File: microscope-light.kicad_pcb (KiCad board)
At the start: 2 copper layers, 72 x 100 mm, 57 parts, among them J1 USB_C_Receptacle_USB2.0, J2 TagConnect_TC2030_SWD, SW1 WARM, SW2 COLD, SW3 BRIGHT, SW4 DIM, U1 SY7200A, U2 SY7200A, U3 STM32F030F4Px, U4 XC6206PxxxMR

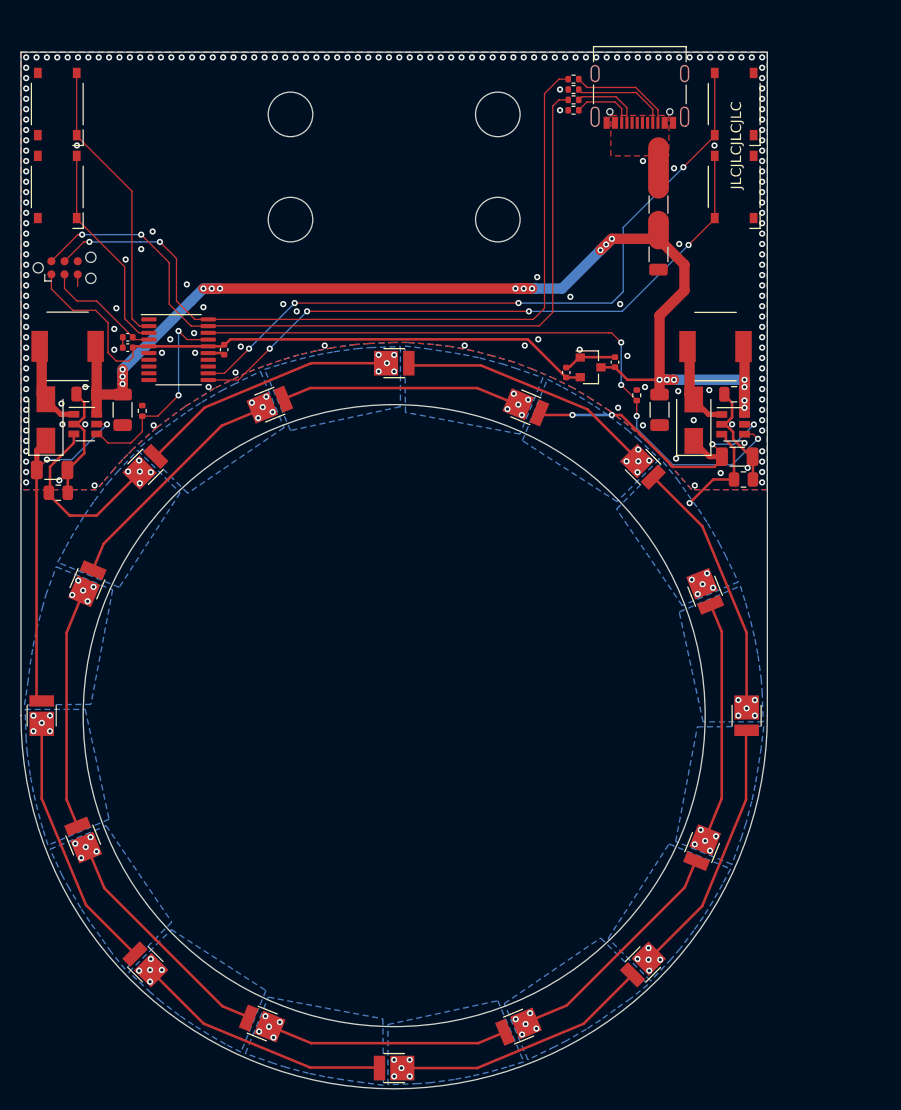
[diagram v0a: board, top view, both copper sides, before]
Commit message: Add fabrication features
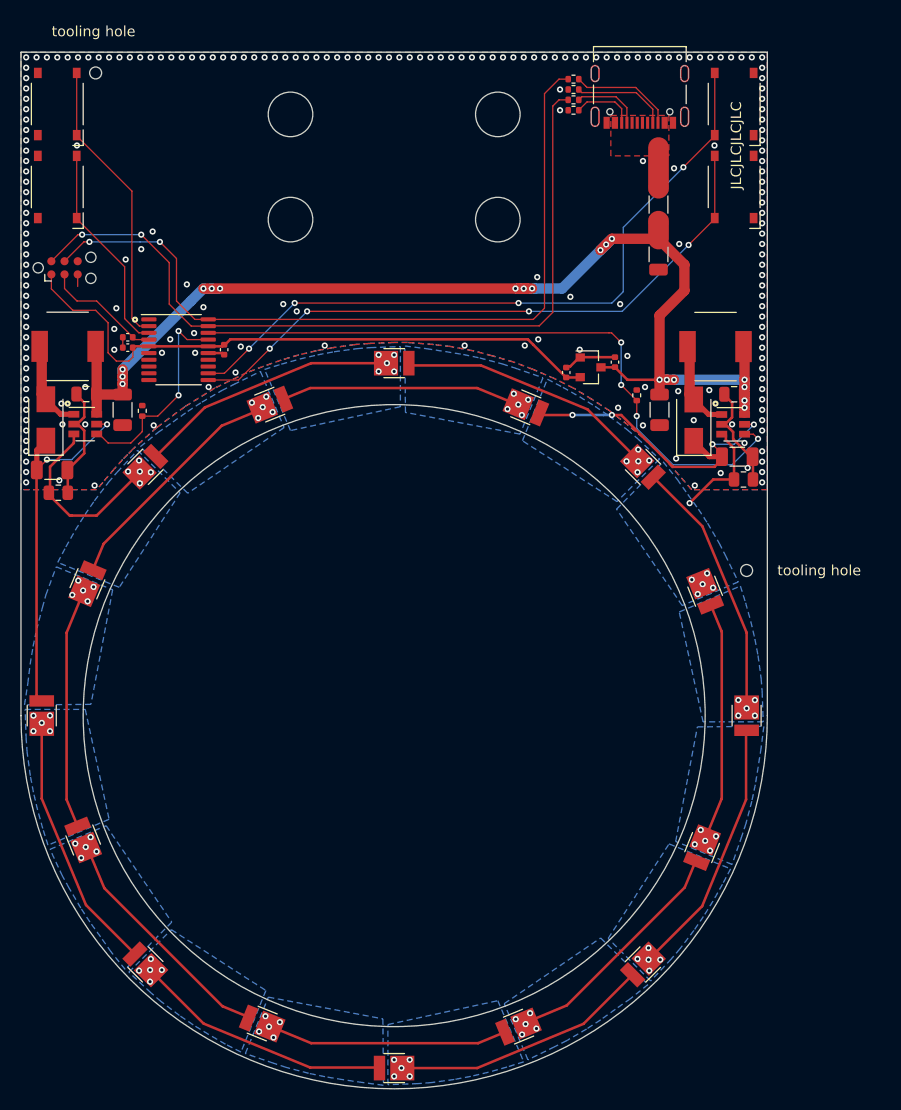
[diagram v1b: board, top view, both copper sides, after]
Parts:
- added H5: ToolingHole, ToolingHole:ToolingHole_JLCSMT, F.Cu at (164.0, 100.0)
- added H6: ToolingHole, ToolingHole:ToolingHole_JLCSMT, F.Cu at (101.2, 52.0)
- D10, D12, D14, D16, D2, D4, D6, D8: value LED -> LEDC
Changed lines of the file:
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@@
   (general
     (thickness 1.6)
-    (drawings 19)
+    (drawings 22)
     (tracks 626)
     (zones 0)
-    (modules 57)
+    (modules 59)
     (nets 50)
   )
@@
     (pcbplotparams
       (layerselection 0x010fc_ffffffff)
-      (usegerberextensions false)
+      (usegerberextensions true)
       (usegerberattributes true)
       (usegerberadvancedattributes true)
-      (creategerberjobfile true)
+      (creategerberjobfile false)
       (excludeedgelayer true)
       (linewidth 0.100000)
@@
       (outputformat 1)
       (mirror false)
-      (drillshape 1)
+      (drillshape 0)
       (scaleselection 1)
-      (outputdirectory ""))
+      (outputdirectory "fab"))
   )
   (net 0 "")
@@
     (add_net "Net-(U3-Pad9)")
   )
+  (module ToolingHole:ToolingHole_JLCSMT (layer F.Cu)
+    (at 101.2 52)
+    (fp_text reference H6 (at 0 0.5) (layer F.SilkS) hide
+      (effects (font (size 1 1) (thickness 0.15)))
+    )
+    (fp_text value ToolingHole (at 0 -0.5) (layer F.Fab)
+      (effects (font (size 1 1) (thickness 0.15)))
+    )
+    (fp_text user "tooling hole" (at -0.2 -4) (layer F.SilkS)
+      (effects (font (size 1 1) (thickness 0.15)))
+    )
+    (pad "" np_thru_hole circle (at 0 0) (size 1.152 1.152) (drill 1.152) (layers *.Cu *.Mask))
+  )
+  (module ToolingHole:ToolingHole_JLCSMT (layer F.Cu)
+    (at 164 100)
+    (fp_text reference H5 (at 0 0.5) (layer F.SilkS) hide
+      (effects (font (size 1 1) (thickness 0.15)))
+    )
+    (fp_text value ToolingHole (at 0 -0.5) (layer F.Fab)
+      (effects (font (size 1 1) (thickness 0.15)))
+    )
+    (fp_text user "tooling hole" (at 7 0) (layer F.SilkS)
+      (effects (font (size 1 1) (thickness 0.15)))
+    )
+    (pad "" np_thru_hole circle (at 0 0) (size 1.152 1.152) (drill 1.152) (layers *.Cu *.Mask))
+  )
   (module Icons:sun (layer B.Cu)
     (at 161.2 70.3)
@@
       (effects (font (size 1 1) (thickness 0.15)))
     )
-    (fp_text value LED (at 0 -0.5 112) (layer F.Fab)
+    (fp_text value LEDC (at 0 -0.5 112) (layer F.Fab)
       (effects (font (size 1 1) (thickness 0.15)))
     )
@@
       (effects (font (size 1 1) (thickness 0.15)))
     )
-    (fp_text value LED (at 0 -0.5 68) (layer F.Fab)
+    (fp_text value LEDC (at 0 -0.5 68) (layer F.Fab)
       (effects (font (size 1 1) (thickness 0.15)))
     )
@@
       (effects (font (size 1 1) (thickness 0.15)))
     )
-    (fp_text value LED (at 0 -0.5 22.5) (layer F.Fab)
+    (fp_text value LEDC (at 0 -0.5 22.5) (layer F.Fab)
       (effects (font (size 1 1) (thickness 0.15)))
     )
@@
       (effects (font (size 1 1) (thickness 0.15)))
     )
-    (fp_text value LED (at 0 -0.5 158) (layer F.Fab)
+    (fp_text value LEDC (at 0 -0.5 158) (layer F.Fab)
       (effects (font (size 1 1) (thickness 0.15)))
     )
@@
       (effects (font (size 1 1) (thickness 0.15)))
     )
-    (fp_text value LED (at 0 -0.5 112) (layer F.Fab)
+    (fp_text value LEDC (at 0 -0.5 112) (layer F.Fab)
       (effects (font (size 1 1) (thickness 0.15)))
     )
@@
       (effects (font (size 1 1) (thickness 0.15)))
     )
-    (fp_text value LED (at 0.000001 -0.5 67) (layer F.Fab)
+    (fp_text value LEDC (at 0.000001 -0.5 67) (layer F.Fab)
       (effects (font (size 1 1) (thickness 0.15)))
     )
@@
       (effects (font (size 1 1) (thickness 0.15)))
     )
-    (fp_text value LED (at 0 -0.5 22) (layer F.Fab)
+    (fp_text value LEDC (at 0 -0.5 22) (layer F.Fab)
       (effects (font (size 1 1) (thickness 0.15)))
     )
@@
       (effects (font (size 1 1) (thickness 0.15)))
     )
-    (fp_text value LED (at 0 -0.5 157.5) (layer F.Fab)
+    (fp_text value LEDC (at 0 -0.5 157.5) (layer F.Fab)
       (effects (font (size 1 1) (thickness 0.15)))
     )
@@
       (effects (font (size 0.8 0.8) (thickness 0.12)))
     )
-    (pad 2 smd roundrect (at 1.475 0 90) (size 1.15 1.8) (layers F.Cu F.Paste F.Mask) (roundrect_rratio 0.217391)
+    (pad 2 smd roundrect (at 1.475 0 90) (size 1.15 1.8) (layers F.Cu F.Paste F.Mask) (roundrect_rratio 0.2173904347826087)
       (net 2 +5V))
-    (pad 1 smd roundrect (at -1.475 0 90) (size 1.15 1.8) (layers F.Cu F.Paste F.Mask) (roundrect_rratio 0.217391)
+    (pad 1 smd roundrect (at -1.475 0 90) (size 1.15 1.8) (layers F.Cu F.Paste F.Mask) (roundrect_rratio 0.2173904347826087)
       (net 1 GND))
     (model ${KISYS3DMOD}/Capacitor_SMD.3dshapes/C_1206_3216Metric.wrl
@@
       (effects (font (size 0.8 0.8) (thickness 0.12)))
     )
-    (pad 2 smd roundrect (at 1.575 0 270) (size 1.05 1.9) (layers F.Cu F.Paste F.Mask) (roundrect_rratio 0.238095)
+    (pad 2 smd roundrect (at 1.575 0 270) (size 1.05 1.9) (layers F.Cu F.Paste F.Mask) (roundrect_rratio 0.2380942857142857)
       (net 2 +5V))
-    (pad 1 smd roundrect (at -1.575 0 270) (size 1.05 1.9) (layers F.Cu F.Paste F.Mask) (roundrect_rratio 0.238095)
+    (pad 1 smd roundrect (at -1.575 0 270) (size 1.05 1.9) (layers F.Cu F.Paste F.Mask) (roundrect_rratio 0.2380942857142857)
       (net 34 "Net-(FB1-Pad1)"))
     (model ${KISYS3DMOD}/Inductor_SMD.3dshapes/L_1206_3216Metric.wrl
@@
       (effects (font (size 0.8 0.8) (thickness 0.12)))
     )
-    (pad 2 smd roundrect (at 1.475 0 90) (size 1.15 1.8) (layers F.Cu F.Paste F.Mask) (roundrect_rratio 0.217391)
+    (pad 2 smd roundrect (at 1.475 0 90) (size 1.15 1.8) (layers F.Cu F.Paste F.Mask) (roundrect_rratio 0.2173904347826087)
       (net 2 +5V))
-    (pad 1 smd roundrect (at -1.475 0 90) (size 1.15 1.8) (layers F.Cu F.Paste F.Mask) (roundrect_rratio 0.217391)
+    (pad 1 smd roundrect (at -1.475 0 90) (size 1.15 1.8) (layers F.Cu F.Paste F.Mask) (roundrect_rratio 0.2173904347826087)
       (net 1 GND))
     (model ${KISYS3DMOD}/Capacitor_SMD.3dshapes/C_1206_3216Metric.wrl
@@
       (effects (font (size 0.8 0.8) (thickness 0.12)))
     )
-    (pad 2 smd roundrect (at 1.475 0 90) (size 1.15 1.8) (layers F.Cu F.Paste F.Mask) (roundrect_rratio 0.217391)
+    (pad 2 smd roundrect (at 1.475 0 90) (size 1.15 1.8) (layers F.Cu F.Paste F.Mask) (roundrect_rratio 0.2173904347826087)
       (net 2 +5V))
-    (pad 1 smd roundrect (at -1.475 0 90) (size 1.15 1.8) (layers F.Cu F.Paste F.Mask) (roundrect_rratio 0.217391)
+    (pad 1 smd roundrect (at -1.475 0 90) (size 1.15 1.8) (layers F.Cu F.Paste F.Mask) (roundrect_rratio 0.2173904347826087)
       (net 1 GND))
     (model ${KISYS3DMOD}/Capacitor_SMD.3dshapes/C_1206_3216Metric.wrl
@@
       (effects (font (size 0.5 0.5) (thickness 0.08)))
     )
-    (pad 2 smd roundrect (at 0.9125 0) (size 1.025 1.4) (layers F.Cu F.Paste F.Mask) (roundrect_rratio 0.243902)
-      (net 1 GND))
-    (pad 1 smd roundrect (at -0.9125 0) (size 1.025 1.4) (layers F.Cu F.Paste F.Mask) (roundrect_rratio 0.243902)
+    (pad 2 smd roundrect (at 0.9125 0) (size 1.025 1.4) (layers F.Cu F.Paste F.Mask) (roundrect_rratio 0.2439014634146341)
+      (net 1 GND))
+    (pad 1 smd roundrect (at -0.9125 0) (size 1.025 1.4) (layers F.Cu F.Paste F.Mask) (roundrect_rratio 0.2439014634146341)
       (net 19 "/LED driver cold/LED-"))
     (model ${KISYS3DMOD}/Resistor_SMD.3dshapes/R_0805_2012Metric.wrl
@@
       (effects (font (size 0.5 0.5) (thickness 0.08)))
     )
-    (pad 1 smd roundrect (at -0.9125 0) (size 1.025 1.4) (layers F.Cu F.Paste F.Mask) (roundrect_rratio 0.243902)
+    (pad 1 smd roundrect (at -0.9125 0) (size 1.025 1.4) (layers F.Cu F.Paste F.Mask) (roundrect_rratio 0.2439014634146341)
       (net 18 "/LED driver warm/LED-"))
-    (pad 2 smd roundrect (at 0.9125 0) (size 1.025 1.4) (layers F.Cu F.Paste F.Mask) (roundrect_rratio 0.243902)
+    (pad 2 smd roundrect (at 0.9125 0) (size 1.025 1.4) (layers F.Cu F.Paste F.Mask) (roundrect_rratio 0.2439014634146341)
       (net 1 GND))
     (model ${KISYS3DMOD}/Resistor_SMD.3dshapes/R_0805_2012Metric.wrl
@@
       (effects (font (size 0.8 0.8) (thickness 0.12)))
     )
-    (pad 2 smd roundrect (at 1.475 0) (size 1.15 1.8) (layers F.Cu F.Paste F.Mask) (roundrect_rratio 0.217391)
-      (net 1 GND))
-    (pad 1 smd roundrect (at -1.475 0) (size 1.15 1.8) (layers F.Cu F.Paste F.Mask) (roundrect_rratio 0.217391)
+    (pad 2 smd roundrect (at 1.475 0) (size 1.15 1.8) (layers F.Cu F.Paste F.Mask) (roundrect_rratio 0.2173904347826087)
+      (net 1 GND))
+    (pad 1 smd roundrect (at -1.475 0) (size 1.15 1.8) (layers F.Cu F.Paste F.Mask) (roundrect_rratio 0.2173904347826087)
       (net 4 "/LED driver cold/LED+"))
     (model ${KISYS3DMOD}/Capacitor_SMD.3dshapes/C_1206_3216Metric.wrl
@@
       (effects (font (size 0.8 0.8) (thickness 0.12)))
     )
-    (pad 1 smd roundrect (at -1.475 0) (size 1.15 1.8) (layers F.Cu F.Paste F.Mask) (roundrect_rratio 0.217391)
+    (pad 1 smd roundrect (at -1.475 0) (size 1.15 1.8) (layers F.Cu F.Paste F.Mask) (roundrect_rratio 0.2173904347826087)
       (net 3 "/LED driver warm/LED+"))
-    (pad 2 smd roundrect (at 1.475 0) (size 1.15 1.8) (layers F.Cu F.Paste F.Mask) (roundrect_rratio 0.217391)
+    (pad 2 smd roundrect (at 1.475 0) (size 1.15 1.8) (layers F.Cu F.Paste F.Mask) (roundrect_rratio 0.2173904347826087)
       (net 1 GND))
     (model ${KISYS3DMOD}/Capacitor_SMD.3dshapes/C_1206_3216Metric.wrl
@@
     )
   )
+  (gr_circle (center 161 83.9) (end 161.1 83.9) (layer F.SilkS) (width 0.4))
+  (gr_circle (center 98.5 83.9) (end 98.6 83.9) (layer F.SilkS) (width 0.4))
+  (gr_circle (center 105 75.8) (end 105.1 75.8) (layer F.SilkS) (width 0.4))
   (gr_text JLCJLCJLCJLC (at 163 59 90) (layer F.SilkS)
     (effects (font (size 1 1) (thickness 0.15)))
